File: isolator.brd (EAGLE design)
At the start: 38.1 x 35.2 mm, 29 parts, among them IC1 TL494BD, Q1 BC817-16LT1SMD, Q2 BC807-16LT1SMD, Q3 BC807-16LT1SMD, Q4 BC817-16LT1SMD

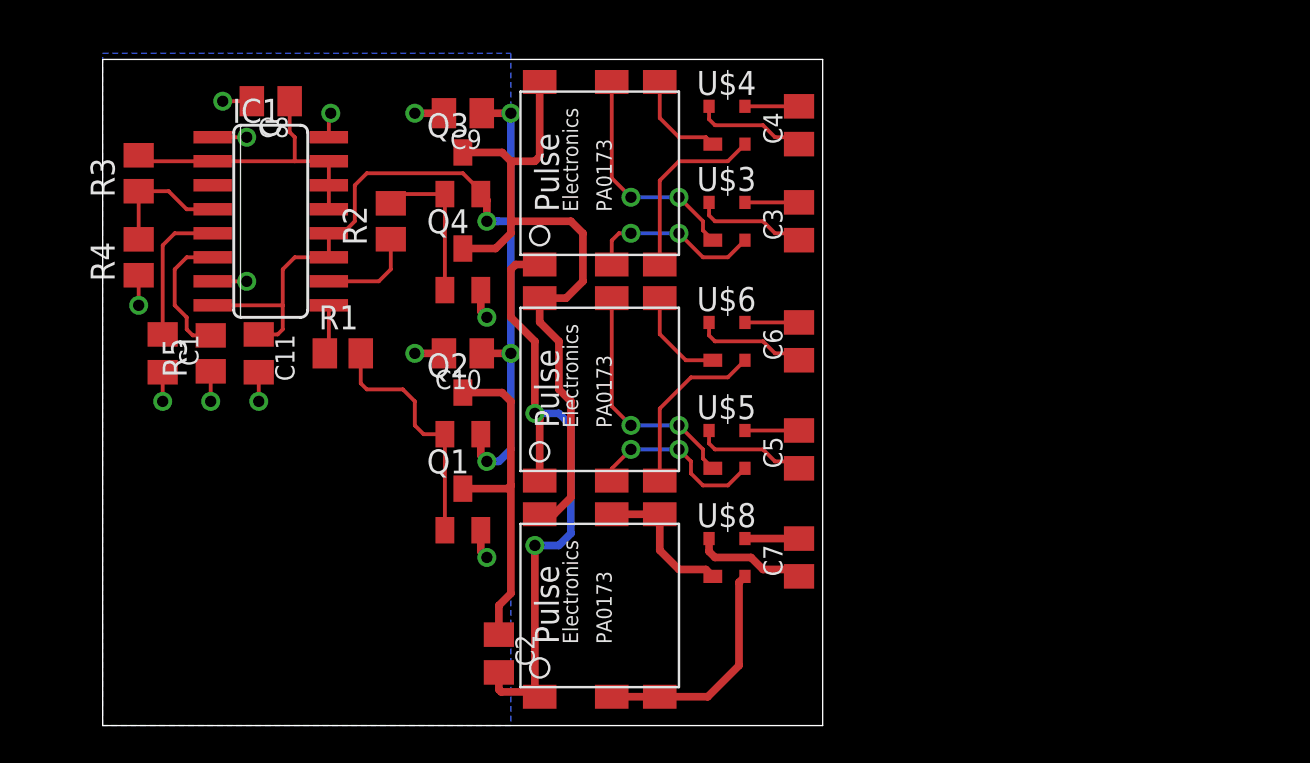
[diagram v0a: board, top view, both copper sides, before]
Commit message: new isolator design
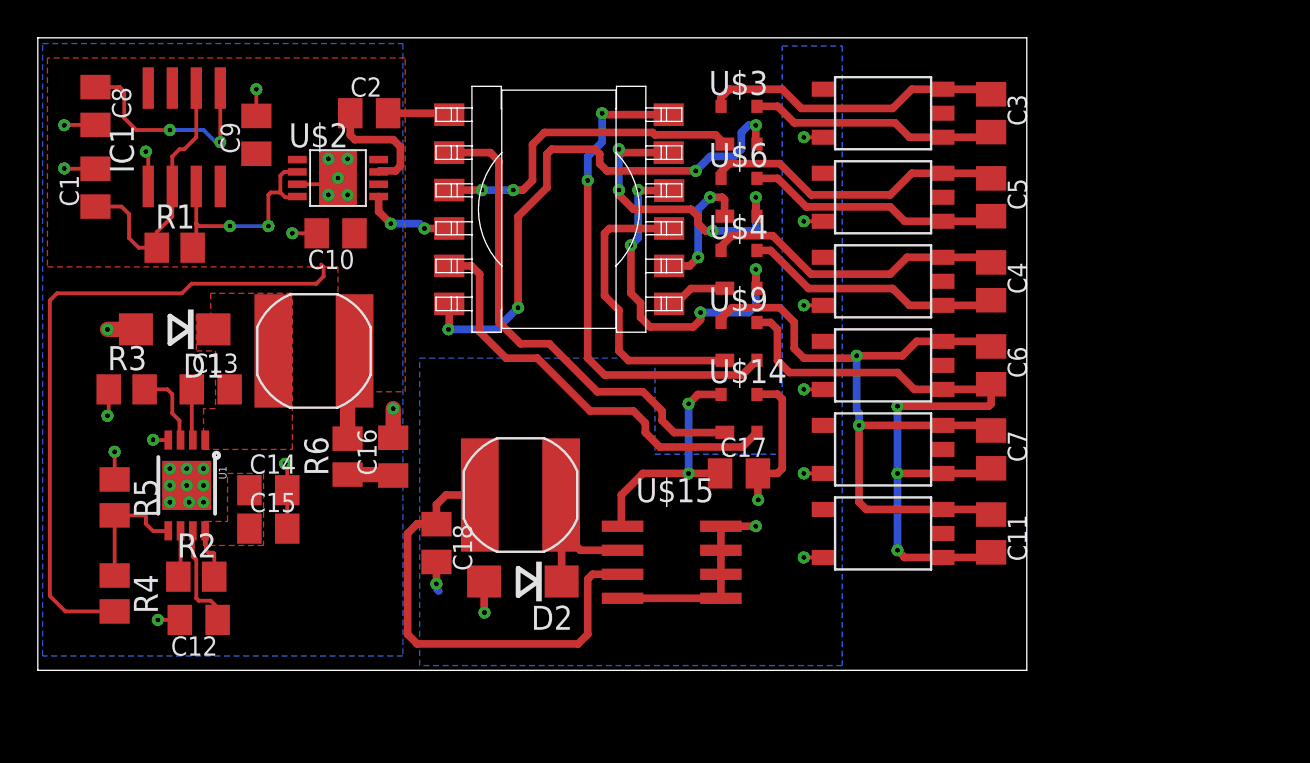
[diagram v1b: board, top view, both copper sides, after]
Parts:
- removed Q1, Q4: BC817-16LT1SMD, transistor-npn:SOT23-BEC
- removed Q2, Q3: BC807-16LT1SMD, transistor-pnp:SOT23-BEC
- added C12, C14, C17: .1u, rcl:C0805K
- added C13: 10n, rcl:C0805K
- added C15: 1u, rcl:C0805K
- added C16, C18: 15u, rcl:C0805K
- added D1, D2: B170-13-F, diode:DO214AC
- added R6: 1, resistor:M0805
- added U$10, U$11, U$12: TLP152, brushlessrage:DIP5-SMD
- added U$13, U$16: SRN6045-101M, brushlessrage:SRN6045
- added U$14, U$9: BAS4002A, utesla:SOT-143
- added U$15: AP1509, brushlessrage:SO8
- added U1: LM5007, SparkFun-PowerIC:MSOP-8-EP
- C1: value (none) -> 3.3n
- C10, C11, C3, C4, C5, C6, C7, C8, C9: value (none) -> .1u
- IC1: value TL494BD -> LM555D; device linear:SO16 -> linear:SO08
- R1, R5: value (none) -> 1k; device rcl:M0805 -> resistor:M0805
- R2: value (none) -> 200k; device rcl:M0805 -> resistor:M0805
- R3: value (none) -> 100k; device rcl:M0805 -> resistor:M0805
- R4: value (none) -> 3.9k; device rcl:M0805 -> resistor:M0805
- U$1: value PA0173 -> HP1; device utesla:PA0173 -> brushlessrage:HP1
- U$2: value PA0173 -> UCC27525DGN; device utesla:PA0173 -> brushlessrage:HTSSOP8DGN
- U$5, U$8: value BAS4002A -> TLP152; device utesla:SOT-143 -> brushlessrage:DIP5-SMD
- U$7: value PA0173 -> TLP152; device utesla:PA0173 -> brushlessrage:DIP5-SMD
- moved C11 39.9 mm to (47.0, 10.2)
- moved U$7 29.9 mm to (41.3, 32.4), turned to 0 degrees
- moved C2 29.4 mm to (14.1, 32.4), turned to 0 degrees
- moved R2 21.4 mm to (4.95, 7.87), turned to 0 degrees
- moved U$8 20.8 mm to (41.3, 27.9)
- moved U$2 18.1 mm to (12.4, 29.0), turned to 270 degrees
- moved R4 17.8 mm to (0.64, 6.99), turned to 270 degrees
- moved C5 16.8 mm to (47.0, 27.9), turned to 270 degrees
- moved C4 13.1 mm to (47.0, 23.5), turned to 270 degrees
- moved U$5 12.1 mm to (41.3, 23.5)
- moved C7 11.7 mm to (47.0, 14.6), turned to 270 degrees
- moved C3 11.7 mm to (47.0, 32.4), turned to 270 degrees
- moved R3 11.4 mm to (1.27, 17.8), turned to 0 degrees
- moved C9 11.0 mm to (8.13, 31.2), turned to 90 degrees
- moved R1 10.5 mm to (3.81, 25.3)
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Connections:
- removed net N$9: C1.1, IC1.5
- removed net VREF: C8.1, IC1.13, IC1.14, IC1.15, IC1.2, R3.2
- new net +3V3: C18.1, U$15.3, U$16.P$2
- new net DGND: C17.2, C18.2, D2.A, U$10.3, U$11.3, U$12.3, U$14.3, U$15.4, U$15.5, U$15.6, U$15.7, U$15.8, U$5.3, U$7.3, U$8.3
- new net DVDD: C17.1, U$14.4, U$15.1
- new net N$31: C12.1, U1.7
- new net N$32: C13.2, D1.C, U$13.P$1, U1.1
- new net N$33: C13.1, U1.2
- new net N$34: R3.2, U1.3
- net +15V: now also IC1.4, R4.2, R6.2, U$13.P$2, U$2.6; no longer C11.1, IC1.11, IC1.12, Q2.E, Q3.E
- net GND: now also C12.2, C14.2, C15.2, C16.2, D1.A, R3.1, U$2.3, U$2.EXP, U1.4, U1.EP; no longer C11.2, IC1.16, IC1.7, Q1.E, Q4.E, R4.1
- net N$1: now also U$1.P$3, U$3.1; no longer C2.2, U$1.1, U$2.1, U$7.1
- net N$10: now also IC1.3, R1.2, U$2.2, U$2.4; no longer C2.1, Q1.C, Q2.C
- net N$11: now also U$1.P$6; no longer U$1.2
- net N$12: now also U$1.P$7, U$4.1; no longer U$1.5, U$3.1
- net N$13: now also C4.1, U$4.4, U$5.6; no longer U$1.3, U$4.2
- net N$14: now also C4.2, U$4.3, U$5.4; no longer U$1.4, U$4.1
- net N$15: now also U$1.P$11, U$6.2; no longer U$2.2, U$5.2
- net N$16: now also U$1.P$8, U$6.1; no longer U$2.5, U$5.1
- net N$17: now also C5.1, U$6.4, U$8.6; no longer U$2.3, U$6.2
- net N$18: now also C5.2, U$6.3, U$8.4; no longer U$2.4, U$6.1
- net N$19: now also U$1.P$12, U$9.2; no longer C3.1, U$3.4
- net N$2: now also C3.1, U$3.4; no longer Q3.C, Q4.C, U$1.6, U$2.6
- net N$20: now also U$1.P$9, U$9.1; no longer C3.2, U$3.3
- net N$21: now also C14.1, C15.1, R2.2, U1.8; no longer C4.1, U$4.4
- net N$22: now also C11.2, C6.2, C7.2, U$10.4, U$11.4, U$12.4, U$9.3; no longer C4.2, U$4.3
- net N$23: now also C16.1, R6.1; no longer C5.1, U$5.4
- net N$24: now also U$1.P$5, U$14.2; no longer C5.2, U$5.3
- net N$25: now also C11.1, C7.1, U$10.6, U$11.6, U$12.6, U$9.4; no longer U$6.4
- net N$26: now also R4.1, R5.2, U1.5; no longer C6.2, U$6.3
- net N$27: now also U$1.P$2, U$14.1; no longer U$7.2, U$7.3, U$8.2
- net N$28: now also R2.1, U1.6; no longer U$7.4, U$7.5, U$8.1
- net N$29: now also D2.C, U$15.2, U$16.P$1; no longer C7.1, U$8.4
- net N$3: now also C3.2, U$3.3, U$7.4; no longer Q1.B, Q2.B, R1.2
- net N$30: now also C2.2, U$1.P$1; no longer C7.2, U$8.3
- net N$4: now also C2.1, U$2.7; no longer Q3.B, Q4.B, R2.2
- net N$5: now also U$1.P$4, U$2.5; no longer IC1.9, R1.1
- net N$6: now also C1.1, IC1.2, IC1.6, R1.1; no longer IC1.10, R2.1
- net N$7: now also U$1.P$10, U$4.2; no longer IC1.4, R3.1, R4.2
- net N$8: now also C8.1, IC1.5; no longer IC1.6, R5.2
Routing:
- net N$22: track 2.86 -> 38.9 mm, vias 0 -> 3
- net N$25: track 5.99 -> 39.3 mm, vias 0 -> 2
- net DGND: track 0.00 -> 27.9 mm, vias 0 -> 10
- net +3V3: track 0.00 -> 25.4 mm
- net N$2: track 37.5 -> 15.9 mm
- net N$19: track 5.99 -> 26.5 mm, vias 0 -> 2
- net N$24: track 2.86 -> 22.6 mm
- net N$11: track 9.37 -> 28.8 mm, vias 2 -> 4
- net N$1: track 34.8 -> 17.2 mm
- net VREF: track 16.0 -> 0.00 mm
- net N$27: track 12.3 -> 26.0 mm
- net N$20: track 2.86 -> 15.9 mm
- net DVDD: track 0.00 -> 13.0 mm, vias 0 -> 2
- net N$7: track 6.85 -> 18.7 mm, vias 0 -> 4
- net +15V: track 50.7 -> 40.2 mm, vias 4 -> 0
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- added copper zone on layer 1, net +15V
- added copper zone on layer 16, net DGND
- added copper zone on layer 1, net N$21
- added copper zone on layer 1, net N$32
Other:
- board size 38.1 x 35.2 mm -> 52.3 x 33.5 mm

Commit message: up-to-date brushlessrage.lbr, updated isolator for send-out
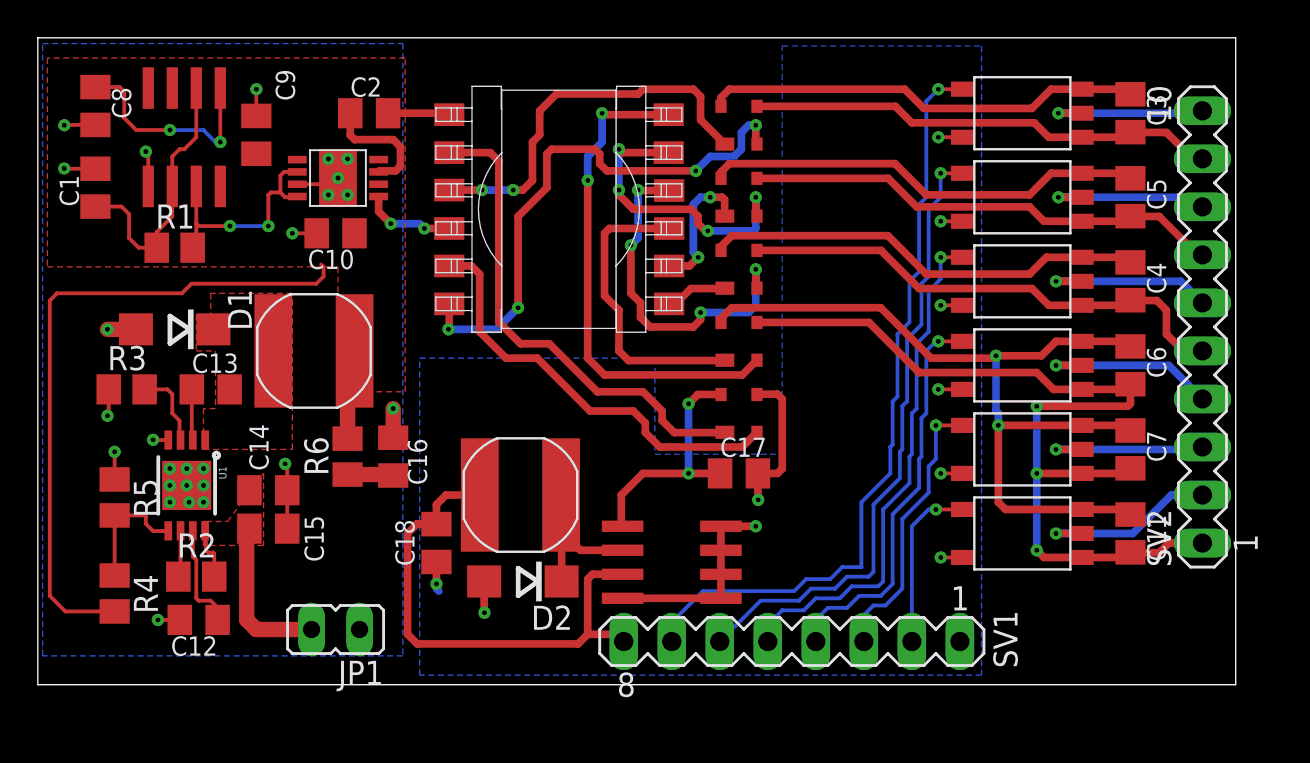
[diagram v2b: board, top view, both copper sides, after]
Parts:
- added JP1: (no value), jumper:JP1
- added SV1: (no value), con-lstb:MA08-1
- added SV2: (no value), con-lstb:MA10-1
- moved C11 7.37 mm to (54.4, 10.2)
- moved C3 7.37 mm to (54.4, 32.4)
- moved C4 7.37 mm to (54.4, 23.5)
- moved C5 7.37 mm to (54.4, 27.9)
- moved C6 7.37 mm to (54.4, 19.1)
- moved C7 7.37 mm to (54.4, 14.6)
- moved U$10 7.37 mm to (48.6, 19.1)
- moved U$11 7.37 mm to (48.6, 14.6)
- moved U$12 7.37 mm to (48.6, 10.2)
- moved U$5 7.37 mm to (48.6, 23.5)
- moved U$7 7.37 mm to (48.6, 32.4)
- moved U$8 7.37 mm to (48.6, 27.9)
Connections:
- removed net N$14: C4.2, U$4.3, U$5.4
- removed net N$18: C5.2, U$6.3, U$8.4
- removed net N$21: C14.1, C15.1, R2.2, U1.8
- removed net N$22: C11.2, C6.2, C7.2, U$10.4, U$11.4, U$12.4, U$9.3
- removed net N$3: C3.2, U$3.3, U$7.4
- new net E1: C3.2, SV2.9, U$3.3, U$7.4
- new net E2: C4.2, SV2.5, U$4.3, U$5.4
- new net E3: C5.2, SV2.7, U$6.3, U$8.4
- new net IN1: SV1.7, U$7.1
- new net IN2: SV1.5, U$5.1
- new net IN3: SV1.6, U$8.1
- new net IN4: SV1.4, U$10.1
- new net IN5: SV1.3, U$11.1
- new net IN6: SV1.2, U$12.1
- new net OUT1: SV2.10, U$7.5
- new net OUT2: SV2.6, U$5.5
- new net OUT3: SV2.8, U$8.5
- new net OUT4: SV2.4, U$10.5
- new net OUT5: SV2.3, U$11.5
- new net OUT6: SV2.2, U$12.5
- new net PGND: C11.2, C6.2, C7.2, SV2.1, U$10.4, U$11.4, U$12.4, U$9.3
- new net VIN: C14.1, C15.1, JP1.2, R2.2, U1.8
- net +3V3: now also SV1.8
- net DGND: now also SV1.1
- net GND: now also JP1.1
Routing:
- net PGND: track 0.00 -> 49.3 mm, vias 0 -> 3
- net IN1: track 0.00 -> 40.5 mm, vias 0 -> 1
- net N$22: track 38.9 -> 0.00 mm, vias 3 -> 0
- net IN3: track 0.00 -> 33.4 mm, vias 0 -> 1
- net IN2: track 0.00 -> 27.5 mm, vias 0 -> 1
- net E2: track 0.00 -> 26.7 mm
- net E3: track 0.00 -> 25.5 mm
- net E1: track 0.00 -> 24.9 mm
- net IN4: track 0.00 -> 21.2 mm, vias 0 -> 1
- net IN5: track 0.00 -> 14.8 mm, vias 0 -> 1
- net N$14: track 13.7 -> 0.00 mm
- net N$18: track 13.4 -> 0.00 mm
- net N$3: track 13.2 -> 0.00 mm
- net VIN: track 0.00 -> 10.6 mm
- net OUT6: track 0.00 -> 9.99 mm, vias 0 -> 1
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- added copper zone on layer 1, net VIN
- removed copper zone on layer 1, net N$21
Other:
- board size 52.3 x 33.5 mm -> 63.4 x 34.2 mm
